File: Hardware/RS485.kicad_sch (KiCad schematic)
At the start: 18 parts, among them J15 Conn_01x05_Pin, J5 Conn_01x02_Male, U9 SP3485EN

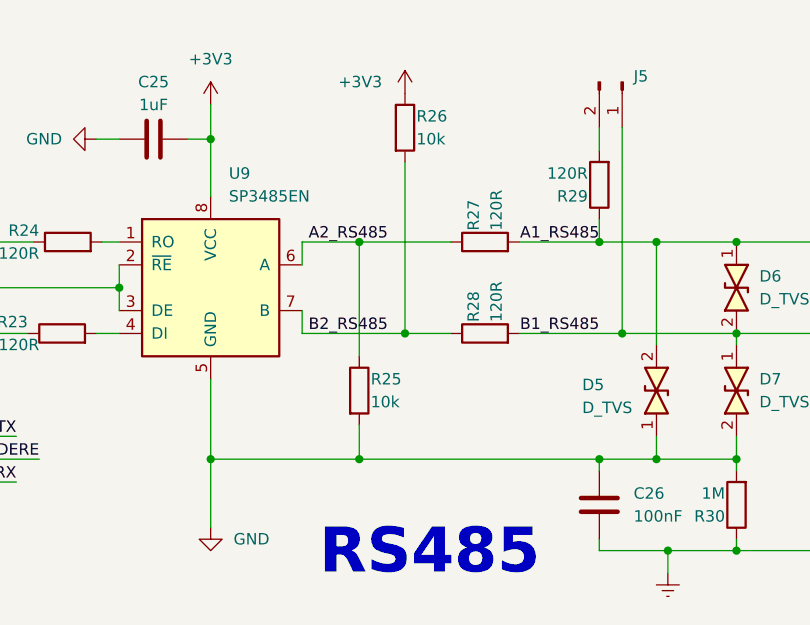
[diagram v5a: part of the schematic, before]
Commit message: complete PCB & fix SCH
fix pull push resistor Pin A, B RS485
diode RTC PCF8564
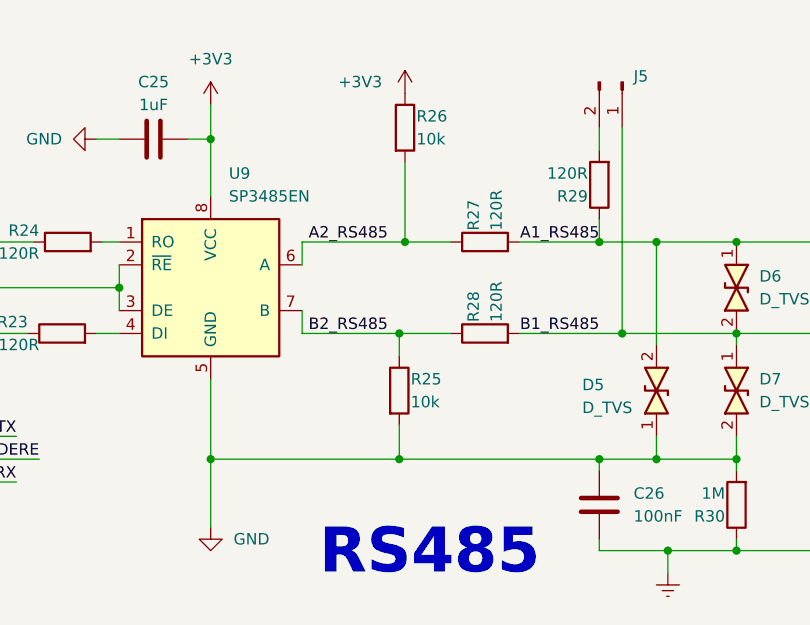
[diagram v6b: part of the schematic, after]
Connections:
- net A2_RS485: now also R26.2; no longer R25.1
- net B2_RS485: now also R25.1; no longer R26.2
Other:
- moved on the sheet: R25
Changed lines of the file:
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@@
   (junction (at 167.64 109.22) (diameter 0) (color 0 0 0 0)
   )
+  (junction (at 130.81 74.93) (diameter 0) (color 0 0 0 0)
+  )
   (junction (at 160.02 109.22) (diameter 0) (color 0 0 0 0)
   )
   (junction (at 152.4 99.06) (diameter 0) (color 0 0 0 0)
   )
-  (junction (at 125.73 99.06) (diameter 0) (color 0 0 0 0)
-  )
   (junction (at 99.06 80.01) (diameter 0) (color 0 0 0 0)
   )
@@
   (junction (at 158.75 74.93) (diameter 0) (color 0 0 0 0)
   )
-  (junction (at 130.81 85.09) (diameter 0) (color 0 0 0 0)
-  )
   (junction (at 109.22 63.5) (diameter 0) (color 0 0 0 0)
   )
-  (junction (at 125.73 74.93) (diameter 0) (color 0 0 0 0)
+  (junction (at 130.175 99.06) (diameter 0) (color 0 0 0 0)
+  )
+  (junction (at 130.175 85.09) (diameter 0) (color 0 0 0 0)
   )
   (bus_entry (at 76.2 96.52) (size -2.54 2.54)
@@
     (stroke (width 0) (type default))
   )
-  (wire (pts (xy 125.73 74.93) (xy 135.89 74.93))
-    (stroke (width 0) (type default))
-  )
   (wire (pts (xy 201.93 81.28) (xy 206.375 81.28))
     (stroke (width 0) (type default))
@@
     (stroke (width 0) (type default))
   )
-  (wire (pts (xy 119.38 74.93) (xy 125.73 74.93))
+  (wire (pts (xy 119.38 74.93) (xy 130.81 74.93))
     (stroke (width 0) (type default))
   )
@@
     (stroke (width 0) (type default))
   )
+  (wire (pts (xy 130.81 66.04) (xy 130.81 74.93))
+    (stroke (width 0) (type default))
+  )
   (wire (pts (xy 203.2 83.82) (xy 206.375 83.82))
     (stroke (width 0) (type default))
@@
     (stroke (width 0) (type default))
   )
+  (wire (pts (xy 130.81 74.93) (xy 135.89 74.93))
+    (stroke (width 0) (type default))
+  )
   (wire (pts (xy 99.06 80.01) (xy 99.06 82.55))
     (stroke (width 0) (type default))
@@
     (stroke (width 0) (type default))
   )
-  (wire (pts (xy 130.81 66.04) (xy 130.81 85.09))
-    (stroke (width 0) (type default))
-  )
   (wire (pts (xy 96.52 63.5) (xy 99.06 63.5))
     (stroke (width 0) (type default))
@@
     (stroke (width 0) (type default))
   )
-  (wire (pts (xy 125.73 99.06) (xy 152.4 99.06))
+  (wire (pts (xy 109.22 99.06) (xy 130.175 99.06))
     (stroke (width 0) (type default))
   )
@@
     (stroke (width 0) (type default))
   )
-  (wire (pts (xy 125.73 74.93) (xy 125.73 87.63))
-    (stroke (width 0) (type default))
-  )
   (wire (pts (xy 119.38 82.55) (xy 119.38 85.09))
     (stroke (width 0) (type default))
@@
     (stroke (width 0) (type default))
   )
+  (wire (pts (xy 130.175 85.09) (xy 130.175 87.63))
+    (stroke (width 0) (type default))
+  )
   (wire (pts (xy 206.375 73.66) (xy 203.2 73.66))
     (stroke (width 0) (type default))
@@
     (stroke (width 0) (type default))
   )
-  (wire (pts (xy 109.22 99.06) (xy 125.73 99.06))
-    (stroke (width 0) (type default))
-  )
   (bus (pts (xy 73.66 104.14) (xy 73.66 101.6))
     (stroke (width 0) (type default))
@@
     (stroke (width 0) (type default))
   )
+  (wire (pts (xy 130.175 99.06) (xy 152.4 99.06))
+    (stroke (width 0) (type default))
+  )
   (wire (pts (xy 152.4 62.23) (xy 152.4 64.77))
     (stroke (width 0) (type default))
@@
     (stroke (width 0) (type default))
   )
-  (wire (pts (xy 130.81 85.09) (xy 135.89 85.09))
-    (stroke (width 0) (type default))
-  )
   (wire (pts (xy 203.2 76.2) (xy 206.375 76.2))
     (stroke (width 0) (type default))
@@
     (stroke (width 0) (type default))
   )
+  (wire (pts (xy 119.38 85.09) (xy 130.175 85.09))
+    (stroke (width 0) (type default))
+  )
   (wire (pts (xy 167.64 107.95) (xy 167.64 109.22))
     (stroke (width 0) (type default))
@@
     (stroke (width 0) (type default))
   )
-  (wire (pts (xy 119.38 85.09) (xy 130.81 85.09))
-    (stroke (width 0) (type default))
-  )
   (wire (pts (xy 109.22 99.06) (xy 109.22 90.17))
     (stroke (width 0) (type default))
   )
-  (wire (pts (xy 125.73 95.25) (xy 125.73 99.06))
+  (wire (pts (xy 130.175 95.25) (xy 130.175 99.06))
     (stroke (width 0) (type default))
   )
@@
   )
   (wire (pts (xy 206.375 78.74) (xy 201.93 78.74))
+    (stroke (width 0) (type default))
+  )
+  (wire (pts (xy 130.175 85.09) (xy 135.89 85.09))
     (stroke (width 0) (type default))
   )
@@
     )
   )
-  (symbol (lib_id "Device:R") (at 125.73 91.44 0) (unit 1)
+  (symbol (lib_id "Device:R") (at 130.175 91.44 0) (unit 1)
     (in_bom yes) (on_board yes) (dnp no)
-    (property "Reference" "R25" (at 127 90.17 0)
-      (effects (font (size 1.27 1.27)) (justify left))
-    )
-    (property "Value" "10k" (at 127 92.71 0)
-      (effects (font (size 1.27 1.27)) (justify left))
-    )
-    (property "Footprint" "IVS_FOOTPRINTS:R0603" (at 123.952 91.44 90)
-      (effects (font (size 1.27 1.27)) hide)
-    )
-    (property "Datasheet" "~" (at 125.73 91.44 0)
-      (effects (font (size 1.27 1.27)) hide)
-    )
+    (property "Reference" "R25" (at 131.445 90.17 0)
+      (effects (font (size 1.27 1.27)) (justify left))
+    )
+    (property "Value" "10k" (at 131.445 92.71 0)
+      (effects (font (size 1.27 1.27)) (justify left))
+    )
+    (property "Footprint" "IVS_FOOTPRINTS:R0603" (at 128.397 91.44 90)
+      (effects (font (size 1.27 1.27)) hide)
+    )
+    (property "Datasheet" "~" (at 130.175 91.44 0)
+      (effects (font (size 1.27 1.27)) hide)
+    )

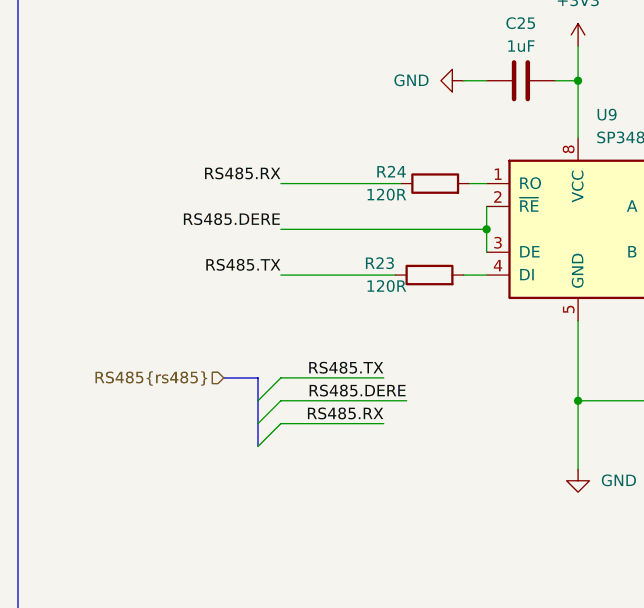
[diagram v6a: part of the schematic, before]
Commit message: add lora, relay, opto, opamp block, led for 74595. Delete RT9193, connect boot0,1 to GND. Fix footprint crystal 8M, 74HC595, IDC pin
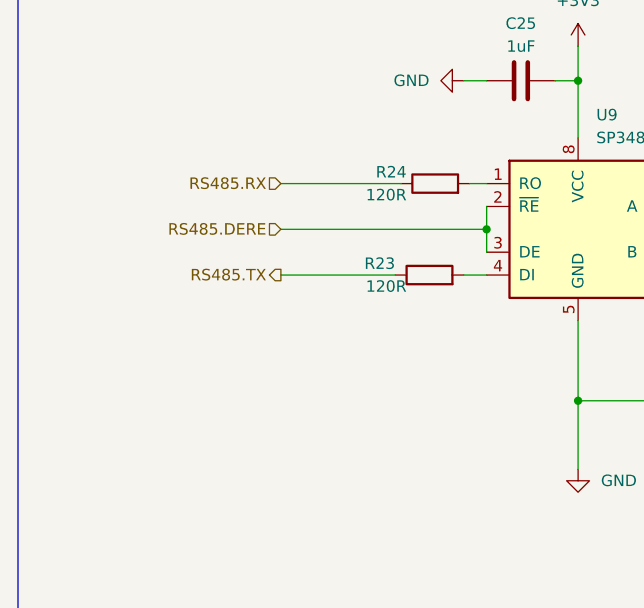
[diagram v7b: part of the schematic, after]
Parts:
- C25, C26: footprint IVS_FOOTPRINTS:C0603 -> IVS_FOOTPRINTS:C_0603
- R23, R24, R25, R26, R27, R28, R29, R30: footprint IVS_FOOTPRINTS:R0603 -> IVS_FOOTPRINTS:R_0603
- U9: footprint Package_SO:SOIC-8_3.9x4.9mm_P1.27mm -> IVS_FOOTPRINTS:SOIC-8_3.9x4.9mm_P1.27mm
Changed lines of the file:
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@@
   (junction (at 130.175 85.09) (diameter 0) (color 0 0 0 0)
   )
-  (bus_entry (at 76.2 96.52) (size -2.54 2.54)
-    (stroke (width 0) (type default))
-  )
-  (bus_entry (at 76.2 99.06) (size -2.54 2.54)
-    (stroke (width 0) (type default))
-  )
-  (bus_entry (at 76.2 101.6) (size -2.54 2.54)
-    (stroke (width 0) (type default))
-  )
   (wire (pts (xy 201.93 81.28) (xy 206.375 81.28))
     (stroke (width 0) (type default))
   )
-  (wire (pts (xy 76.2 96.52) (xy 87.63 96.52))
-    (stroke (width 0) (type default))
-  )
   (wire (pts (xy 152.4 72.39) (xy 152.4 74.93))
     (stroke (width 0) (type default))
@@
     (stroke (width 0) (type default))
   )
-  (bus (pts (xy 73.66 104.14) (xy 73.66 101.6))
-    (stroke (width 0) (type default))
-  )
   (wire (pts (xy 99.06 77.47) (xy 99.06 80.01))
     (stroke (width 0) (type default))
@@
     (stroke (width 0) (type default))
   )
-  (wire (pts (xy 76.2 101.6) (xy 87.63 101.6))
-    (stroke (width 0) (type default))
-  )
   (wire (pts (xy 203.2 83.82) (xy 203.2 109.22))
     (stroke (width 0) (type default))
@@
     (stroke (width 0) (type default))
   )
-  (bus (pts (xy 73.66 99.06) (xy 73.66 96.52))
-    (stroke (width 0) (type default))
-  )
   (wire (pts (xy 76.2 80.01) (xy 99.06 80.01))
     (stroke (width 0) (type default))
@@
     (stroke (width 0) (type default))
   )
-  (bus (pts (xy 69.85 96.52) (xy 73.66 96.52))
-    (stroke (width 0) (type default))
-  )
   (wire (pts (xy 109.22 63.5) (xy 109.22 69.85))
     (stroke (width 0) (type default))
@@
     (stroke (width 0) (type default))
   )
-  (wire (pts (xy 76.2 99.06) (xy 90.17 99.06))
-    (stroke (width 0) (type default))
-  )
   (wire (pts (xy 158.75 99.06) (xy 167.64 99.06))
     (stroke (width 0) (type default))
@@
   )
   (wire (pts (xy 203.2 109.22) (xy 167.64 109.22))
-    (stroke (width 0) (type default))
-  )
-  (bus (pts (xy 73.66 101.6) (xy 73.66 99.06))
     (stroke (width 0) (type default))
   )
@@
     (effects (font (size 1.27 1.27)) (justify left bottom))
   )
-  (label "RS485.RX" (at 87.63 101.6 180) (fields_autoplaced)
-    (effects (font (size 1.27 1.27)) (justify right bottom))
-  )
   (label "A_RS485" (at 191.77 74.93 0) (fields_autoplaced)
     (effects (font (size 1.27 1.27)) (justify left bottom))
   )
-  (label "RS485.TX" (at 76.2 85.09 180) (fields_autoplaced)
-    (effects (font (size 1.27 1.27)) (justify right bottom))
-  )
-  (label "RS485.RX" (at 76.2 74.93 180) (fields_autoplaced)
-    (effects (font (size 1.27 1.27)) (justify right bottom))
-  )
-  (label "RS485.DERE" (at 90.17 99.06 180) (fields_autoplaced)
-    (effects (font (size 1.27 1.27)) (justify right bottom))
-  )
-  (label "RS485.DERE" (at 76.2 80.01 180) (fields_autoplaced)
-    (effects (font (size 1.27 1.27)) (justify right bottom))
-  )
-  (label "RS485.TX" (at 87.63 96.52 180) (fields_autoplaced)
-    (effects (font (size 1.27 1.27)) (justify right bottom))
-  )
   (label "A1_RS485" (at 152.4 74.93 180) (fields_autoplaced)
     (effects (font (size 1.27 1.27)) (justify right bottom))
@@
     (effects (font (size 1.27 1.27)) (justify right bottom))
   )
-  (hierarchical_label "RS485{rs485}" (shape input) (at 69.85 96.52 180) (fields_autoplaced)
+  (hierarchical_label "RS485.TX" (shape output) (at 76.2 85.09 180) (fields_autoplaced)
     (effects (font (size 1.27 1.27)) (justify right))
   )
+  (hierarchical_label "RS485.DERE" (shape input) (at 76.2 80.01 180) (fields_autoplaced)
+    (effects (font (size 1.27 1.27)) (justify right))
+  )
+  (hierarchical_label "RS485.RX" (shape input) (at 76.2 74.93 180) (fields_autoplaced)
+    (effects (font (size 1.27 1.27)) (justify right))
+  )
   (symbol (lib_id "power:GND") (at 96.52 63.5 270) (unit 1)
     (in_bom yes) (on_board yes) (dnp no) (fields_autoplaced)
@@
       (effects (font (size 1.27 1.27)) (justify left))
     )
-    (property "Footprint" "IVS_FOOTPRINTS:R0603" (at 139.7 86.868 90)
+    (property "Footprint" "IVS_FOOTPRINTS:R_0603" (at 139.7 86.868 90)
       (effects (font (size 1.27 1.27)) hide)
     )
@@
       (effects (font (size 1.27 1.27)))
     )
-    (property "Footprint" "IVS_FOOTPRINTS:C0603" (at 106.68 62.5348 0)
+    (property "Footprint" "IVS_FOOTPRINTS:C_0603" (at 106.68 62.5348 0)
       (effects (font (size 1.27 1.27)) hide)
     )
@@
       (effects (font (size 1.27 1.27)) (justify left))
     )
-    (property "Footprint" "IVS_FOOTPRINTS:R0603" (at 139.7 76.708 90)
+    (property "Footprint" "IVS_FOOTPRINTS:R_0603" (at 139.7 76.708 90)
       (effects (font (size 1.27 1.27)) hide)
     )
@@
       (effects (font (size 1.27 1.27)) (justify left))
     )
-    (property "Footprint" "IVS_FOOTPRINTS:R0603" (at 128.397 91.44 90)
+    (property "Footprint" "IVS_FOOTPRINTS:R_0603" (at 128.397 91.44 90)
       (effects (font (size 1.27 1.27)) hide)
     )
@@
       (effects (font (size 1.27 1.27)) (justify left))
     )
-    (property "Footprint" "IVS_FOOTPRINTS:R0603" (at 169.418 104.14 90)
+    (property "Footprint" "IVS_FOOTPRINTS:R_0603" (at 169.418 104.14 90)
       (effects (font (size 1.27 1.27)) hide)
     )
@@
       (effects (font (size 1.27 1.27)) (justify right))
     )
-    (property "Footprint" "IVS_FOOTPRINTS:C0603" (at 151.4348 100.33 0)
+    (property "Footprint" "IVS_FOOTPRINTS:C_0603" (at 151.4348 100.33 0)
       (effects (font (size 1.27 1.27)) hide)
     )
@@
       (effects (font (size 1.27 1.27)) (justify left))
     )
-    (property "Footprint" "IVS_FOOTPRINTS:R0603" (at 92.71 86.868 90)
+    (property "Footprint" "IVS_FOOTPRINTS:R_0603" (at 92.71 86.868 90)
       (effects (font (size 1.27 1.27)) hide)
     )
@@
       (effects (font (size 1.27 1.27)) (justify left))
     )
-    (property "Footprint" "IVS_FOOTPRINTS:R0603" (at 93.345 76.708 90)
+    (property "Footprint" "IVS_FOOTPRINTS:R_0603" (at 93.345 76.708 90)
       (effects (font (size 1.27 1.27)) hide)
     )
@@
       (effects (font (size 1.27 1.27)) (justify left))
     )
-    (property "Footprint" "IVS_FOOTPRINTS:R0603" (at 129.032 62.23 90)
+    (property "Footprint" "IVS_FOOTPRINTS:R_0603" (at 129.032 62.23 90)
       (effects (font (size 1.27 1.27)) hide)
     )
@@
       (effects (font (size 1.27 1.27)) (justify left))
     )
-    (property "Footprint" "IVS_FOOTPRINTS:R0603" (at 154.178 68.58 90)
+    (property "Footprint" "IVS_FOOTPRINTS:R_0603" (at 154.178 68.58 90)
       (effects (font (size 1.27 1.27)) hide)
     )
@@
       (effects (font (size 1.27 1.27)) (justify left))
     )
-    (property "Footprint" "Package_SO:SOIC-8_3.9x4.9mm_P1.27mm" (at 135.89 88.9 0)
+    (property "Footprint" "IVS_FOOTPRINTS:SOIC-8_3.9x4.9mm_P1.27mm" (at 135.89 88.9 0)
       (effects (font (size 1.27 1.27) italic) hide)
     )
